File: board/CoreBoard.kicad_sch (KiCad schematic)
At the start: 6 parts

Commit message: rev2 progress
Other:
- sheet Fans ports: added none; removed PWM2, Tach2
- sheet Lighting ports: added BStrip, GStrip, RStrip; removed none
- sheet Teensy ports: added BStrip, GStrip, RStrip; removed FPWM2, FTACH2
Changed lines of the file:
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@@
 	(wire
 		(pts
-			(xy 233.68 181.61) (xy 246.38 181.61)
+			(xy 247.65 176.53) (xy 248.92 176.53)
 		)
 		(stroke
@@
 	(wire
 		(pts
-			(xy 233.68 179.07) (xy 246.38 179.07)
+			(xy 245.11 173.99) (xy 248.92 173.99)
 		)
 		(stroke
@@
 	(wire
 		(pts
+			(xy 233.68 186.69) (xy 245.11 186.69)
+		)
+		(stroke
+			(width 0)
+			(type default)
+		)
+	)
+	(wire
+		(pts
 			(xy 170.18 96.52) (xy 170.18 114.3)
 		)
@@
 	(wire
 		(pts
+			(xy 233.68 184.15) (xy 243.84 184.15)
+		)
+		(stroke
+			(width 0)
+			(type default)
+		)
+	)
+	(wire
+		(pts
 			(xy 233.68 96.52) (xy 246.38 96.52)
 		)
@@
 	(wire
 		(pts
+			(xy 247.65 181.61) (xy 233.68 181.61)
+		)
+		(stroke
+			(width 0)
+			(type default)
+		)
+	)
+	(wire
+		(pts
 			(xy 170.18 190.5) (xy 176.53 190.5)
 		)
@@
 	(wire
 		(pts
+			(xy 246.38 182.88) (xy 248.92 182.88)
+		)
+		(stroke
+			(width 0)
+			(type default)
+		)
+	)
+	(wire
+		(pts
 			(xy 172.72 119.38) (xy 172.72 99.06)
 		)
@@
 	(wire
 		(pts
+			(xy 243.84 185.42) (xy 248.92 185.42)
+		)
+		(stroke
+			(width 0)
+			(type default)
+		)
+	)
+	(wire
+		(pts
 			(xy 233.68 132.08) (xy 246.38 132.08)
 		)
@@
 	(wire
 		(pts
+			(xy 245.11 186.69) (xy 245.11 187.96)
+		)
+		(stroke
+			(width 0)
+			(type default)
+		)
+	)
+	(wire
+		(pts
+			(xy 243.84 184.15) (xy 243.84 185.42)
+		)
+		(stroke
+			(width 0)
+			(type default)
+		)
+	)
+	(wire
+		(pts
 			(xy 233.68 129.54) (xy 246.38 129.54)
 		)
@@
 	(wire
 		(pts
+			(xy 233.68 189.23) (xy 246.38 189.23)
+		)
+		(stroke
+			(width 0)
+			(type default)
+		)
+	)
+	(wire
+		(pts
 			(xy 170.18 190.5) (xy 170.18 210.82)
 		)
@@
 	(wire
 		(pts
-			(xy 167.64 140.97) (xy 176.53 140.97)
-		)
-		(stroke
-			(width 0)
-			(type default)
-		)
-	)
-	(wire
-		(pts
 			(xy 160.02 210.82) (xy 160.02 180.34)
 		)
@@
 	(wire
 		(pts
-			(xy 167.64 143.51) (xy 176.53 143.51)
-		)
-		(stroke
-			(width 0)
-			(type default)
-		)
-	)
-	(wire
-		(pts
 			(xy 143.51 156.21) (xy 176.53 156.21)
 		)
@@
 	(wire
 		(pts
+			(xy 245.11 187.96) (xy 248.92 187.96)
+		)
+		(stroke
+			(width 0)
+			(type default)
+		)
+	)
+	(wire
+		(pts
+			(xy 245.11 173.99) (xy 245.11 179.07)
+		)
+		(stroke
+			(width 0)
+			(type default)
+		)
+	)
+	(wire
+		(pts
+			(xy 246.38 189.23) (xy 246.38 182.88)
+		)
+		(stroke
+			(width 0)
+			(type default)
+		)
+	)
+	(wire
+		(pts
 			(xy 148.59 170.18) (xy 148.59 210.82)
 		)
@@
 		)
 	)
+	(wire
+		(pts
+			(xy 247.65 176.53) (xy 247.65 181.61)
+		)
+		(stroke
+			(width 0)
+			(type default)
+		)
+	)
 	(polyline
 		(pts
@@
 		(pts
 			(xy 165.1 185.42) (xy 176.53 185.42)
+		)
+		(stroke
+			(width 0)
+			(type default)
+		)
+	)
+	(wire
+		(pts
+			(xy 245.11 179.07) (xy 233.68 179.07)
 		)
 		(stroke
@@
 			)
 		)
-		(pin "PWM2" input
-			(at 167.64 143.51 0)
-			(effects
-				(font
-					(size 1.27 1.27)
-				)
-				(justify right)
-			)
-		)
 		(pin "Tach1" output
 			(at 167.64 134.62 0)
-			(effects
-				(font
-					(size 1.27 1.27)
-				)
-				(justify right)
-			)
-		)
-		(pin "Tach2" output
-			(at 167.64 140.97 0)
 			(effects
 				(font
@@
 			)
 		)
-		(pin "FPWM2" output
-			(at 176.53 143.51 180)
-			(effects
-				(font
-					(size 1.27 1.27)
-				)
-				(justify left)
-			)
-		)
 		(pin "FTACH1" input
 			(at 176.53 134.62 180)
@@
 			)
 		)
-		(pin "FTACH2" input
-			(at 176.53 140.97 180)
-			(effects
-				(font
-					(size 1.27 1.27)
-				)
-				(justify left)
-			)
-		)
 		(pin "RGB_Strip" output
 			(at 233.68 181.61 0)
@@
 		(pin "Lighting_Panel" output
 			(at 233.68 179.07 0)
+			(effects
+				(font
+					(size 1.27 1.27)
+				)
+				(justify right)
+			)
+		)
+		(pin "BStrip" output
+			(at 233.68 184.15 0)
+			(effects
+				(font
+					(size 1.27 1.27)
+				)
+				(justify right)
+			)
+		)
+		(pin "GStrip" output
+			(at 233.68 186.69 0)
+			(effects
+				(font
+					(size 1.27 1.27)
+				)
+				(justify right)
+			)
+		)
+		(pin "RStrip" output
+			(at 233.68 189.23 0)
 			(effects
 				(font
@@
 	)
 	(sheet
-		(at 246.38 171.45)
-		(size 22.86 16.51)
+		(at 248.92 171.45)
+		(size 22.86 19.685)
 		(exclude_from_sim no)
 		(in_bom yes)
@@
 		)
 		(property "Sheetname" "Lighting"
-			(at 246.38 170.7384 0)
+			(at 248.92 170.7384 0)
 			(effects
 				(font
@@
 		)
 		(property "Sheetfile" "lighting.kicad_sch"
-			(at 246.38 188.5446 0)
+			(at 248.92 191.7196 0)
 			(effects
 				(font
@@
 		)
 		(pin "Lighting_Panel" input
-			(at 246.38 179.07 180)
+			(at 248.92 173.99 180)
 			(effects
 				(font
@@
 		)
 		(pin "RGB_Strip" input
-			(at 246.38 181.61 180)
-			(effects
-				(font
+			(at 248.92 176.53 180)
+			(effects
+				(font
+					(size 1.27 1.27)
+				)
+				(justify left)
+			)
+		)
+		(pin "BStrip" input
+			(at 248.92 185.42 180)
+			(effects
+				(font
+					(size 1.27 1.27)
+				)
+				(justify left)
+			)
+		)
+		(pin "GStrip" input
+			(at 248.92 187.96 180)
+			(effects
+				(font
+					(size 1.27 1.27)
+				)
+				(justify left)
+			)
+		)
+		(pin "RStrip" input
+			(at 248.92 182.88 180)
+			(effects
+				(font

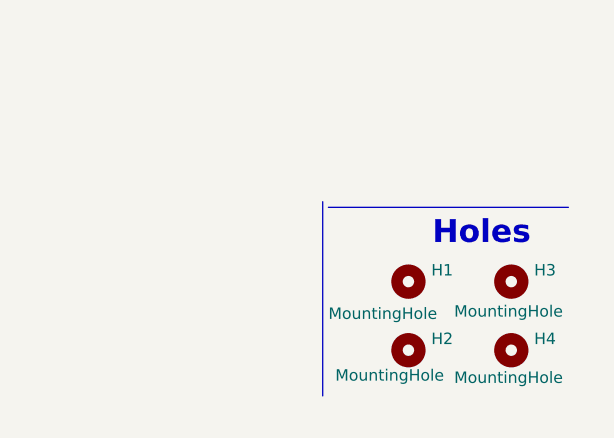
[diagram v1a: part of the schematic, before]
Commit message: Add plated mounting holes and buck converter
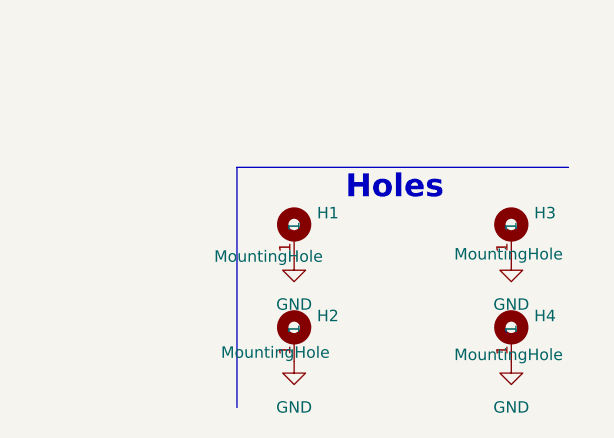
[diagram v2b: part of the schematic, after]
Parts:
- H1, H2, H3, H4: footprint MRDT_Drill_Holes:4_40_Hole -> MRDT_Drill_Holes:4_40_Hole_Pad_Via; symbol Mechanical:MountingHole -> MRDT_Connectors:4_40_Mounting_Hole_Pad; now in the parts list
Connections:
- new net GND: H1.1, H2.1, H3.1, H4.1
